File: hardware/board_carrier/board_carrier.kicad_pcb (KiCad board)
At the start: 2 copper layers, 40 x 36.5 mm, 18 parts, among them J3 Conn_02x06_Top_Bottom, U1 TJA1051T-3, U2 LM78M05_TO252, U3 f042_wideband_module

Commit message: board_carrier: PCB generator (bottom-side analog stage, placer, Freerouting with upstream tracks locked) - work in progress, 3 nets unrouted
Co-Authored-By: Claude Opus 5.5 <noreply@anthropic.com>
Claude-Session: https://claude.ai/code/session_01PSzkdckEqA8UiAsfxtaSyg
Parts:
- added C11: 100n, C_0603_1608Metric, B.Cu at (63.4, 86.6)
- added C12: 100n, C_0603_1608Metric, B.Cu at (64.4, 84.4)
- added C13: 100n, C_0603_1608Metric, B.Cu at (54.8, 87.2)
- added C14: 100n, C_0603_1608Metric, B.Cu at (66.2, 87.2)
- added C15: 1n, C_0603_1608Metric, B.Cu at (65.8, 73.8)
- added C16: 10u, C_1206_3216Metric, B.Cu at (66.6, 71.2)
- added C17: 100n, C_0603_1608Metric, B.Cu at (69.4, 84.6)
- added D3: 1N4148W, D_SOD-123, B.Cu at (59.4, 75.8)
- added D4: 1N4148W, D_SOD-123, B.Cu at (57.8, 80.4)
- added D5: 18V, D_SOD-123, B.Cu at (53.6, 70.8)
- added JP1: TEST, SolderJumper-2_P1.3mm_Open_RoundedPad1.0x1.5mm, B.Cu at (51.2, 81.0)
- added JP2: CAN_TERM, SolderJumper-2_P1.3mm_Open_RoundedPad1.0x1.5mm, B.Cu at (50.8, 84.6)
- added R10: 120, R_0603_1608Metric, B.Cu at (57.4, 69.2)
- added R3: 100k, R_0603_1608Metric, B.Cu at (53.8, 80.8)
- added R4: 3.3k, R_0603_1608Metric, B.Cu at (53.8, 84.4)
- added R5: 3.3k, R_0603_1608Metric, B.Cu at (62.8, 88.8)
- added R6: 68k, R_0603_1608Metric, B.Cu at (64.4, 82.2)
- added R7: 100k, R_0603_1608Metric, B.Cu at (61.6, 82.8)
- added R8: 330, R_0603_1608Metric, B.Cu at (60.2, 72.0)
- added R9: 1k, R_0603_1608Metric, B.Cu at (50.4, 88.0)
- added U4: 74LVC1G125, SOT-353_SC-70-5, B.Cu at (56.6, 83.4)
- added U5: REF3030, SOT-23, B.Cu at (58.8, 86.8)
- added U6: LM2904, SOIC-8_3.9x4.9mm_P1.27mm, B.Cu at (65.0, 78.0)
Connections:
- J3 pad 5: unconnected-(J3-Pad5) -> /AOUT
- J3 pad 7: unconnected-(J3-Pad7) -> GND
- U3 pad 3: unconnected-(U3-Pad3) -> /AOUT_PWM
- U3 pad 4: unconnected-(U3-Pad4) -> /TEST_SEL2
- U3 pad 8: /Boot0 -> unconnected-(U3-Boot0-Pad8)
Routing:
- net /VOP12: track 0.00 -> 70.5 mm
- net /CAN_TERM: track 0.00 -> 60.2 mm, vias 0 -> 4
- net /LSU_Heater+: track 44.5 -> 81.7 mm, vias 2 -> 3
- net /AOUT: track 0.00 -> 29.1 mm
- net /AOUT_INN: track 0.00 -> 21.1 mm
- net /AOUT_PWM: track 0.00 -> 20.4 mm
- net /AOUT_OA: track 0.00 -> 15.6 mm
- net /AOUT_F1: track 0.00 -> 12.8 mm
- net /VREF3: track 0.00 -> 8.90 mm
- net /AOUT_BUF: track 0.00 -> 8.73 mm, vias 0 -> 2
- net /TEST_SEL2: track 0.00 -> 8.06 mm
- net /AOUT_F2: track 0.00 -> 6.30 mm, vias 0 -> 1
- net /CAN_L: track 39.2 -> 40.8 mm, vias 3 -> 4
- net /U6B_FB: track 0.00 -> 1.27 mm
- net +5V: track 50.3 -> 50.1 mm, vias 1 -> 2
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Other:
- rule solder_mask_min_width: 0.25 -> 0.1
- board text added: "AOUT"
- board text added: "TEST"
- board text added: "VBAT"
- board text added: "v1.1-aout"
- board text removed: "12V"
- board text removed: "RX"
- board text removed: "TX"
- board text removed: "nRESET"
- board text removed: "v1.1"

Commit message: board_carrier: annealing placer, GND fan-out and +5V tap vias, grid finisher after Freerouting, 0402 passives; 0 new DRC violations, 3 connections open (WIP)
work: checks/drc_vs_upstream.py (DRC minus upstream's baseline, in run_all), HANDOFF.md replaced with run history r6-r16 and the last raw output, STATE updated, R8/R9 power rating flagged for the audit

Co-Authored-By: Claude Opus 5.5 <noreply@anthropic.com>
Claude-Session: https://claude.ai/code/session_01PSzkdckEqA8UiAsfxtaSyg
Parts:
- C11, C12, C13, C14, C15: footprint C_0603_1608Metric -> C_0402_1005Metric
- D3, D4: value 1N4148W -> 1N4148WS; footprint D_SOD-123 -> D_SOD-323
- R10, R3, R4, R5, R7: footprint R_0603_1608Metric -> R_0402_1005Metric
- moved C16 17.9 mm to (62.0, 88.5), turned to 180 degrees
- moved D5 17.8 mm to (52.2, 88.5), turned to 180 degrees
- moved JP2 15.3 mm to (52.0, 69.3), turned to 90 degrees
- moved C12 7.92 mm to (57.4, 80.7), turned to 90 degrees
- moved R10 7.80 mm to (49.6, 69.1), turned to -90 degrees
- moved C11 5.67 mm to (57.8, 87.5), turned to 180 degrees
- moved R5 5.10 mm to (61.4, 83.9), turned to 90 degrees
- moved C17 4.56 mm to (67.4, 88.7), turned to -90 degrees
- moved C14 4.18 mm to (63.4, 84.1), turned to 0 degrees
- moved U4 3.69 mm to (54.6, 80.3)
- moved R9 2.64 mm to (52.0, 85.9), turned to 0 degrees
- moved R3 2.50 mm to (51.4, 80.1), turned to 180 degrees
- moved R8 2.25 mm to (61.4, 73.9), turned to 180 degrees
- moved U5 2.14 mm to (58.4, 84.7)
- moved R4 2.06 mm to (55.4, 83.1), turned to -90 degrees
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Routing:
- net /CAN_TERM: track 60.2 -> 2.54 mm, vias 4 -> 0
- net /VOP12: track 70.5 -> 26.4 mm
- net /LSU_Heater+: track 81.7 -> 50.9 mm, vias 3 -> 2
- net +5V: track 50.1 -> 72.5 mm, vias 2 -> 4
- net /CAN_L: track 40.8 -> 61.1 mm, vias 4 -> 3
- net GND: track 0.00 -> 12.8 mm, vias 68 -> 75
- net /AOUT_OA: track 15.6 -> 4.07 mm
- net /AOUT_INN: track 21.1 -> 13.6 mm
- net /VREF3: track 8.90 -> 2.60 mm
- net /AOUT_BUF: track 8.73 -> 3.70 mm, vias 2 -> 0
- net /AOUT_F2: track 6.30 -> 1.81 mm, vias 1 -> 0
- net /AOUT: track 29.1 -> 25.7 mm
- net /TEST_SEL2: track 8.06 -> 5.52 mm
- net /AOUT_PWM: track 20.4 -> 22.5 mm
- net /CAN_H: track 39.6 -> 41.0 mm
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
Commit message: board_carrier: negotiated routing (PathFinder) of the analog stage's nets before Freerouting, GND pour pieces joined, vias kept out of SMD pads; 0 new DRC violations, 1 connection open (D3 to +5V)
work: checks/via_in_pad.py in run_all

Co-Authored-By: Claude Opus 5.5 <noreply@anthropic.com>
Claude-Session: https://claude.ai/code/session_01PSzkdckEqA8UiAsfxtaSyg
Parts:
- moved C13 6.99 mm to (62.2, 87.3)
- moved R4 5.97 mm to (60.0, 86.9), turned to 0 degrees
- moved C16 5.69 mm to (67.6, 87.5), turned to 0 degrees
- moved C17 4.44 mm to (66.8, 84.3), turned to 0 degrees
- moved C11 3.82 mm to (60.6, 84.9), turned to -90 degrees
- moved U4 3.81 mm to (54.4, 84.1), turned to -90 degrees
- moved D5 3.69 mm to (55.8, 87.7), turned to 0 degrees
- moved C12 3.30 mm to (54.2, 81.5), turned to 180 degrees
- moved R3 3.21 mm to (54.6, 79.9), turned to 0 degrees
- moved R6 3.20 mm to (61.8, 82.3)
- moved R7 2.83 mm to (64.8, 82.3), turned to 0 degrees
- moved JP1 2.15 mm to (51.2, 80.9)
- moved D4 1.46 mm to (58.0, 80.3), turned to 180 degrees
- moved R9 1.46 mm to (50.6, 86.3)
- moved R5 1.13 mm to (62.2, 84.7)
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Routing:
- net /LSU_Heater+: track 50.9 -> 86.3 mm, vias 2 -> 4
- net /AOUT_OA: track 4.07 -> 33.5 mm
- net +5V: track 72.5 -> 61.6 mm
- net /AOUT_F1: track 14.2 -> 3.56 mm
- net /AOUT_F2: track 1.81 -> 10.6 mm
- net /VREF3: track 2.60 -> 10.3 mm, vias 0 -> 2
- net /CAN_L: track 61.1 -> 54.2 mm
- net /AOUT_PWM: track 22.5 -> 27.0 mm
- net /AOUT_BUF: track 3.70 -> 8.12 mm
- net /AOUT: track 25.7 -> 22.7 mm
- net /AOUT_INN: track 13.6 -> 11.3 mm
- net /TEST_SEL2: track 5.52 -> 4.58 mm
- net GND: track 12.8 -> 13.7 mm, vias 75 -> 79

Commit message: board_carrier: last open connection closed (D3 +5V to U2 pin 3, C1 GND via, C2 solid pour) via close_d3_link in the generator; 0 new DRC violations, 0 open vs upstream, 0 new vias in pads
work: whatif_route.py (candidate tracks scored on a scratch copy), report.py status page, audit hand-off in AUDIT.md, HANDOFF replaced, lessons, artifact-pipeline note; CLAUDE.md gains the gtest commands and the test-build quirk

Co-Authored-By: Claude Sonnet 5.5 <noreply@anthropic.com>
Claude-Session: https://claude.ai/code/session_013ZVt2aLpmrSY8uzxABcZfb
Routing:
- net +5V: track 61.6 -> 65.6 mm
- net /LSU_Heater+: track 86.3 -> 88.5 mm
- net GND: track 13.7 -> 14.6 mm, vias 79 -> 80

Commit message: board_carrier: board grown 15 mm (40.0 x 51.5 mm), analog stage in the new strip, R11 470R at J3-5 so a 12 V wiring fault can't back-feed +5V; 0 new DRC, 0 open, 0 vias in pads, 0 layout-review triggers (r36)
- gen_carrier_pcb: grow_board(), stage targets in the strip, upstream tracks all kept (REROUTE empty), bypass/Cf caps
  tied to their pins (C17 2.1 mm from U6 pin 8, was 4.5), CAN terminator moved off the output's corridor (r35)
- checks/layout_review.py (new, in checks.json): coupling, return paths, GND pour, as numbers
- sim/stability.sh topology D (R11): stable, 0.46 % low into 100k
- AGENTS.md rules 7-8: no assumed engineering decisions; layout changes re-checked by measurement
- docs/carrier.md: layout, review checklist, grounding analysis (J3-7 doc claim corrected), bring-up test A4
- RELEASE_ASSESSMENT/AUDIT/STATE/HANDOFF/LESSONS updated; new owner questions D7-D9

Co-Authored-By: Claude Opus 5.5 <noreply@anthropic.com>
Claude-Session: https://claude.ai/code/session_013ZVt2aLpmrSY8uzxABcZfb
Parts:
- added R11: 470, R_1206_3216Metric, B.Cu at (53.2, 97.2)
- moved C15 26.5 mm to (56.2, 99.0), turned to 90 degrees
- moved JP2 25.9 mm to (43.6, 93.8)
- moved R10 24.4 mm to (46.0, 93.2)
- moved C11 22.9 mm to (48.6, 104.4), turned to 0 degrees
- moved C13 22.4 mm to (46.0, 102.8)
- moved R7 20.9 mm to (55.4, 101.0), turned to 180 degrees
- moved C12 20.4 mm to (46.0, 100.2), turned to 90 degrees
- moved U6 19.9 mm to (61.0, 97.6)
- moved U5 19.8 mm to (49.0, 101.6), turned to 0 degrees
- moved R8 19.7 mm to (56.6, 93.0)
- moved C14 19.2 mm to (58.0, 103.0), turned to 180 degrees
- moved C17 18.4 mm to (63.4, 102.4), turned to -90 degrees
- moved JP1 18.2 mm to (43.6, 97.4), turned to 180 degrees
- moved R9 18.0 mm to (66.2, 95.2), turned to -90 degrees
- moved R3 17.4 mm to (46.8, 95.4), turned to 180 degrees
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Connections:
- J3 pad 5: /AOUT -> /AOUT_J
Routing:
- net /AOUT_J: track 0.00 -> 46.2 mm, vias 0 -> 2
- net /TEST_SEL2: track 4.58 -> 31.7 mm, vias 0 -> 4
- net /AOUT_OA: track 33.5 -> 8.85 mm, vias 0 -> 2
- net /LSU_Heater+: track 88.5 -> 65.9 mm, vias 4 -> 2
- net /VOP12: track 26.4 -> 9.75 mm
- net /AOUT_F1: track 3.56 -> 18.8 mm, vias 0 -> 2
- net /CAN_H: track 40.9 -> 54.7 mm, vias 1 -> 2
- net /AOUT: track 22.7 -> 13.3 mm
- net /AOUT_BUF: track 8.12 -> 1.62 mm
- net +5V: track 65.6 -> 70.5 mm, vias 4 -> 5
- net /VREF3: track 10.3 -> 5.62 mm, vias 2 -> 0
- net /AOUT_PWM: track 27.0 -> 30.9 mm, vias 0 -> 3
- net /AOUT_INN: track 11.3 -> 7.68 mm
- net /AOUT_F2: track 10.6 -> 7.55 mm
- net /CAN_TERM: track 2.54 -> 1.54 mm
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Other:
- board size 40 x 36.5 mm -> 40 x 51.5 mm

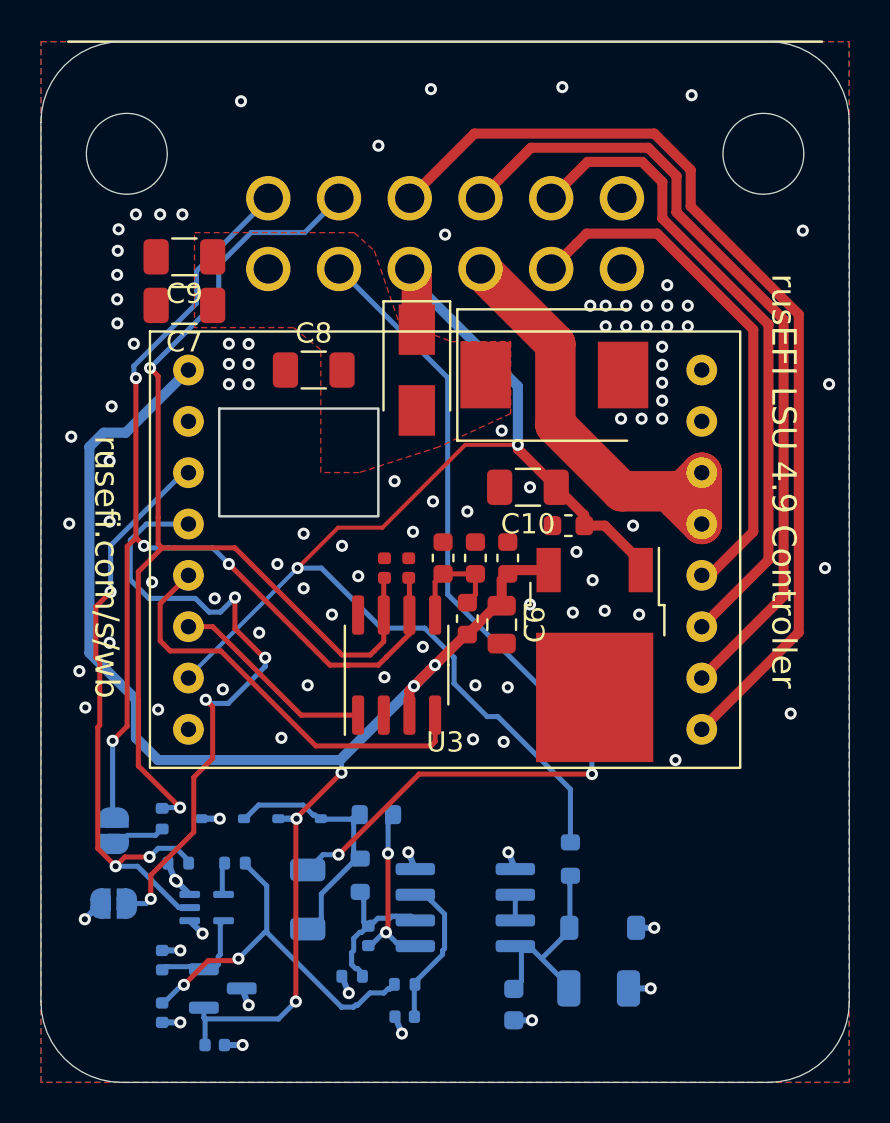
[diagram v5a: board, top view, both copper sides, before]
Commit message: board_carrier: r37: stage on the top (D9), feedback from J3-5 after R11 (C2), R9 1206 (D1), M3 holes (D8); 0 new DRC, 0 open, layout review clean. work: raw DRC advisory per D2, module-identical check
Co-Authored-By: Claude Opus 5.5 <noreply@anthropic.com>
Claude-Session: https://claude.ai/code/session_013ZVt2aLpmrSY8uzxABcZfb
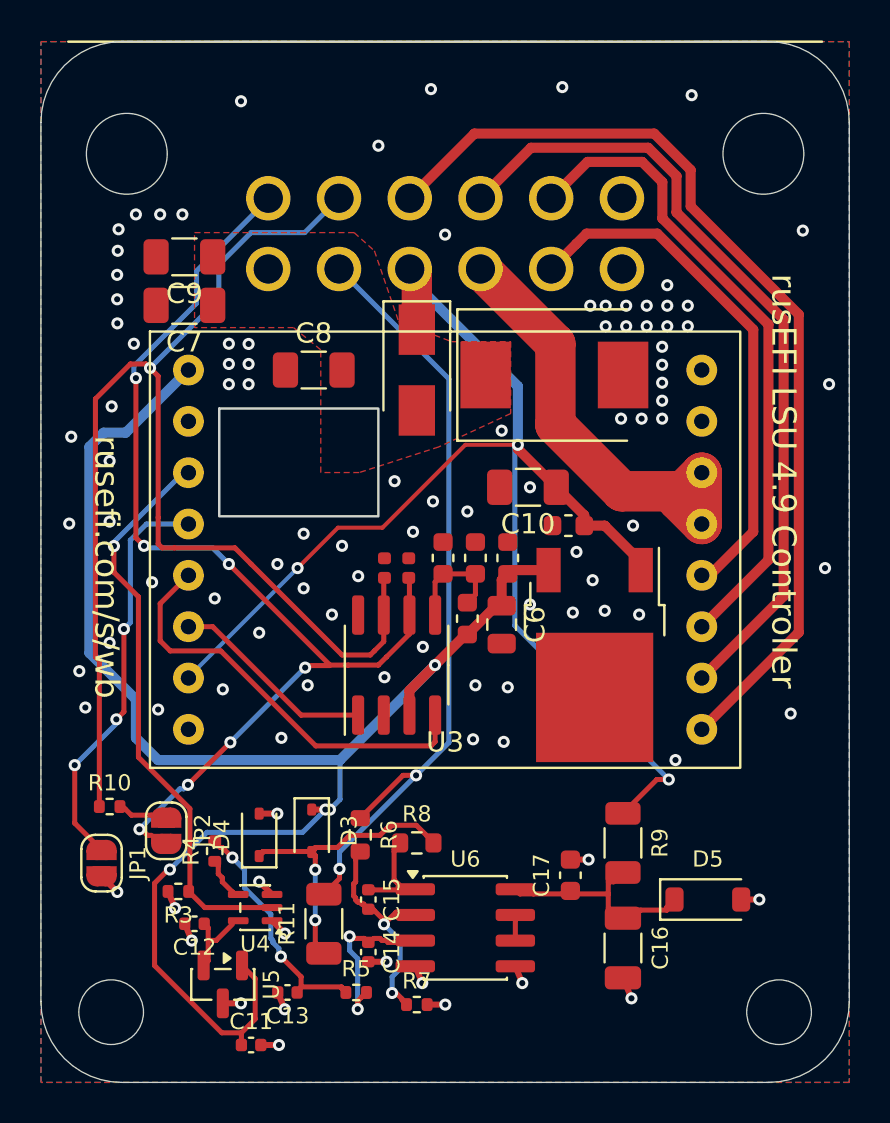
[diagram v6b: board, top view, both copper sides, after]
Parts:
- added H1: MountingHole_3.2mm_M3, MountingHole_3.2mm_M3, F.Cu at (43.5, 102.8)
- added H2: MountingHole_3.2mm_M3, MountingHole_3.2mm_M3, F.Cu at (76.5, 102.8)
- C11, C12, C13, C14, C15, C16, C17, D3, D4, D5, JP1, JP2, R10, R11, R3, R4, R5, R6, R7, R8, U4, U5, U6: moved to F.Cu
- R9: footprint R_0603_1608Metric -> R_1206_3216Metric; moved to F.Cu
- moved C17 6.99 mm to (66.2, 96.0), turned to 90 degrees
- moved C13 6.28 mm to (52.2, 101.8), turned to 180 degrees
- moved D5 5.39 mm to (73.0, 97.2)
- moved C14 3.67 mm to (56.2, 99.8), turned to -90 degrees
- moved R7 3.49 mm to (58.6, 102.4), turned to 0 degrees
- moved R9 2.72 mm to (68.8, 94.4)
- moved R10 2.67 mm to (43.4, 92.6), turned to 0 degrees
- moved JP2 2.60 mm to (46.2, 93.8), turned to -90 degrees
- moved R8 2.44 mm to (58.6, 94.4), turned to 0 degrees
- moved R5 2.43 mm to (55.6, 101.8)
- moved C12 2.41 mm to (47.6, 98.4), turned to 180 degrees
- moved U4 2.40 mm to (50.6, 97.6), turned to 180 degrees
- moved C16 2.33 mm to (68.8, 99.6), turned to -90 degrees
- moved JP1 2.09 mm to (43.0, 95.4), turned to -90 degrees
- moved R6 2.00 mm to (55.8, 94.0)
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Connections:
- R6 pad 1: /AOUT -> /AOUT_J
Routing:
- net /TEST_SEL2: track 31.7 -> 20.2 mm, vias 4 -> 3
- net /CAN_H: track 54.7 -> 63.3 mm, vias 2 -> 1
- net +5V: track 70.5 -> 78.3 mm, vias 5 -> 4
- net /AOUT_F1: track 18.8 -> 11.8 mm
- net /AOUT_J: track 46.2 -> 39.4 mm
- net /AOUT_OA: track 8.85 -> 4.57 mm, vias 2 -> 0
- net /AOUT_INN: track 7.68 -> 11.4 mm, vias 0 -> 2
- net /AOUT_PWM: track 30.9 -> 28.4 mm, vias 3 -> 1
- net /VREF3: track 5.62 -> 3.77 mm
- net /AOUT: track 13.3 -> 15.0 mm, vias 0 -> 2
- net /LSU_Heater+: track 65.9 -> 67.2 mm, vias 2 -> 3
- net /VOP12: track 9.75 -> 11.0 mm
- net /CAN_TERM: track 1.54 -> 2.52 mm
- net /CAN_L: track 53.5 -> 52.7 mm, vias 4 -> 7
- net /AOUT_F2: track 7.55 -> 8.35 mm, vias 0 -> 2
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
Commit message: board_carrier: r38: merge same-net vias drilled too close (hole_to_hole hidden as a warning since about r26). work: DRC delta counts fab-relevant warnings; lesson
Co-Authored-By: Claude Opus 5.5 <noreply@anthropic.com>
Claude-Session: https://claude.ai/code/session_013ZVt2aLpmrSY8uzxABcZfb
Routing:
- net +5V: track 78.3 -> 78.0 mm, vias 4 -> 3

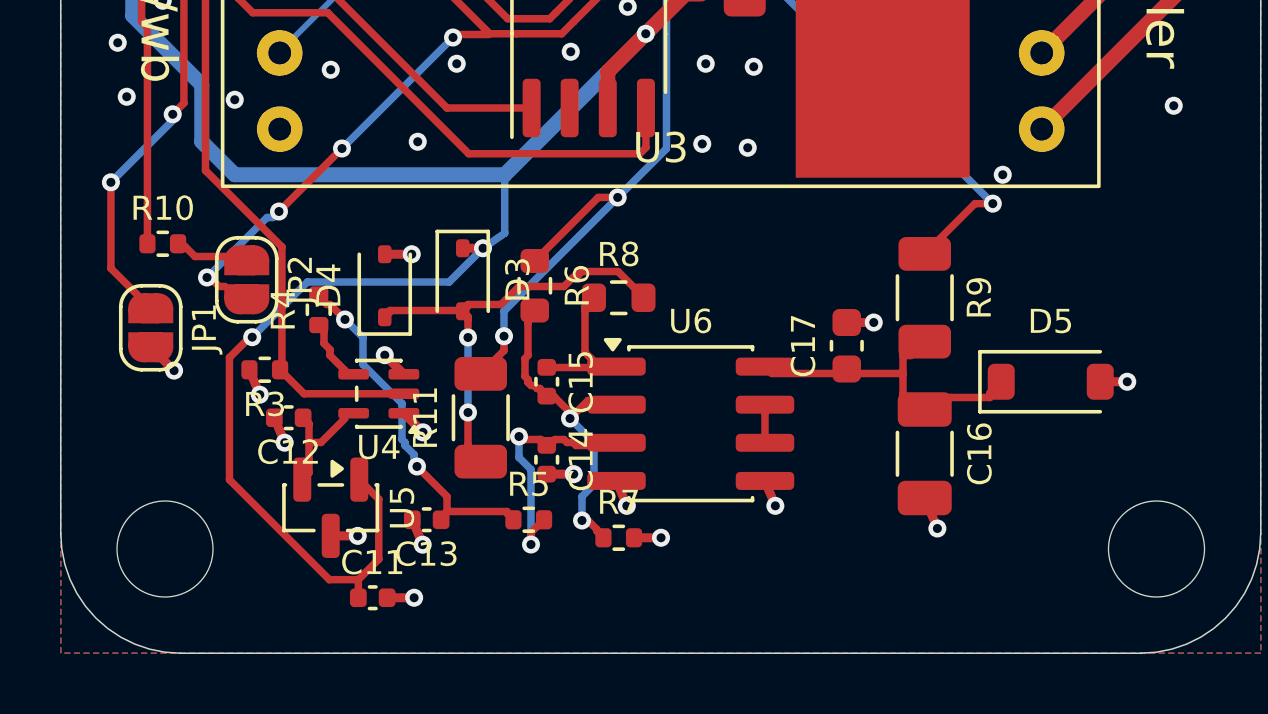
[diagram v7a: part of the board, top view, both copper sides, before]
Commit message: board_carrier: r39: silkscreen pass (gen/silk.py): readable labels that belong to their part, jumper function labels TEST and 120R
Co-Authored-By: Claude Opus 5.5 <noreply@anthropic.com>
Claude-Session: https://claude.ai/code/session_013ZVt2aLpmrSY8uzxABcZfb
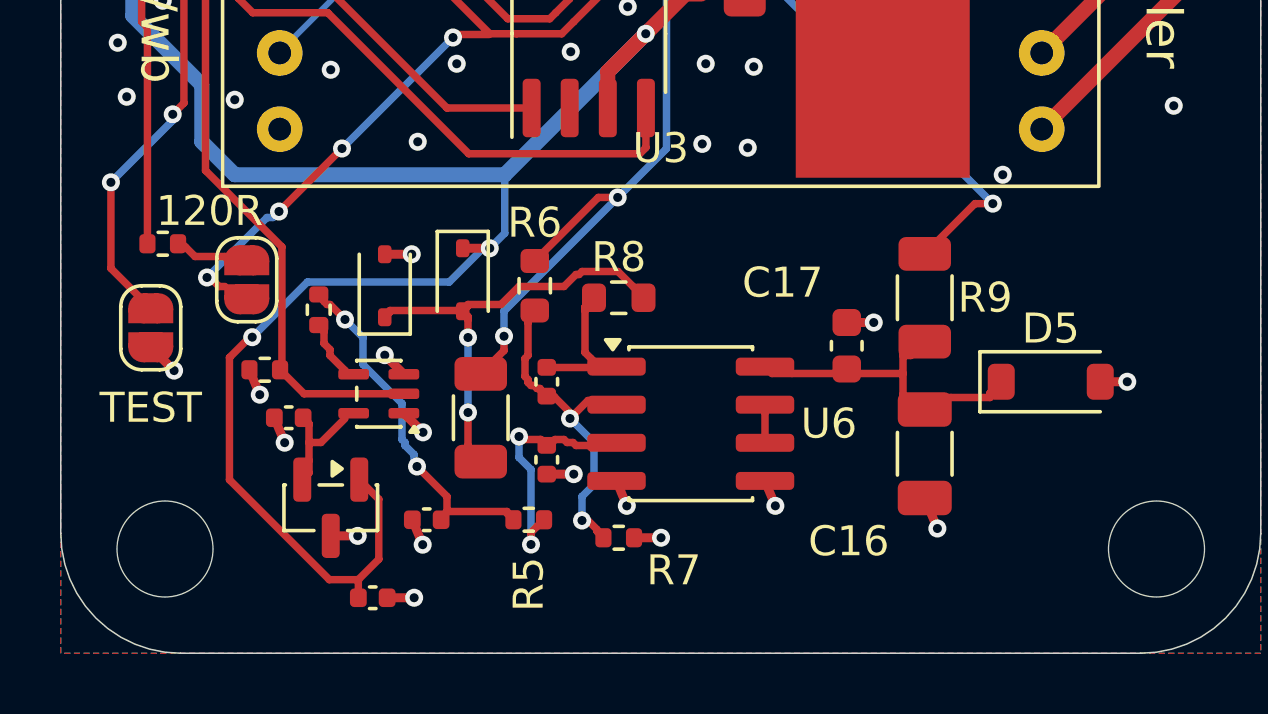
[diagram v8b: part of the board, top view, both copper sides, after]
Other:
- board text added: "120R"
